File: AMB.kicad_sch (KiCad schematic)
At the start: 14 parts, among them U11 EPC2152, U12 EPC2152

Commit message: updated layouts, added motor
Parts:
- renumbered C95 to C119, C96 to C120, C97 to C121, C98 to C122, C99 to C123, C100 to C124, C101 to C125, C102 to C126, R71 to R127, R72 to R128, R73 to R129, R74 to R130, U12 to U10, U11 to U9

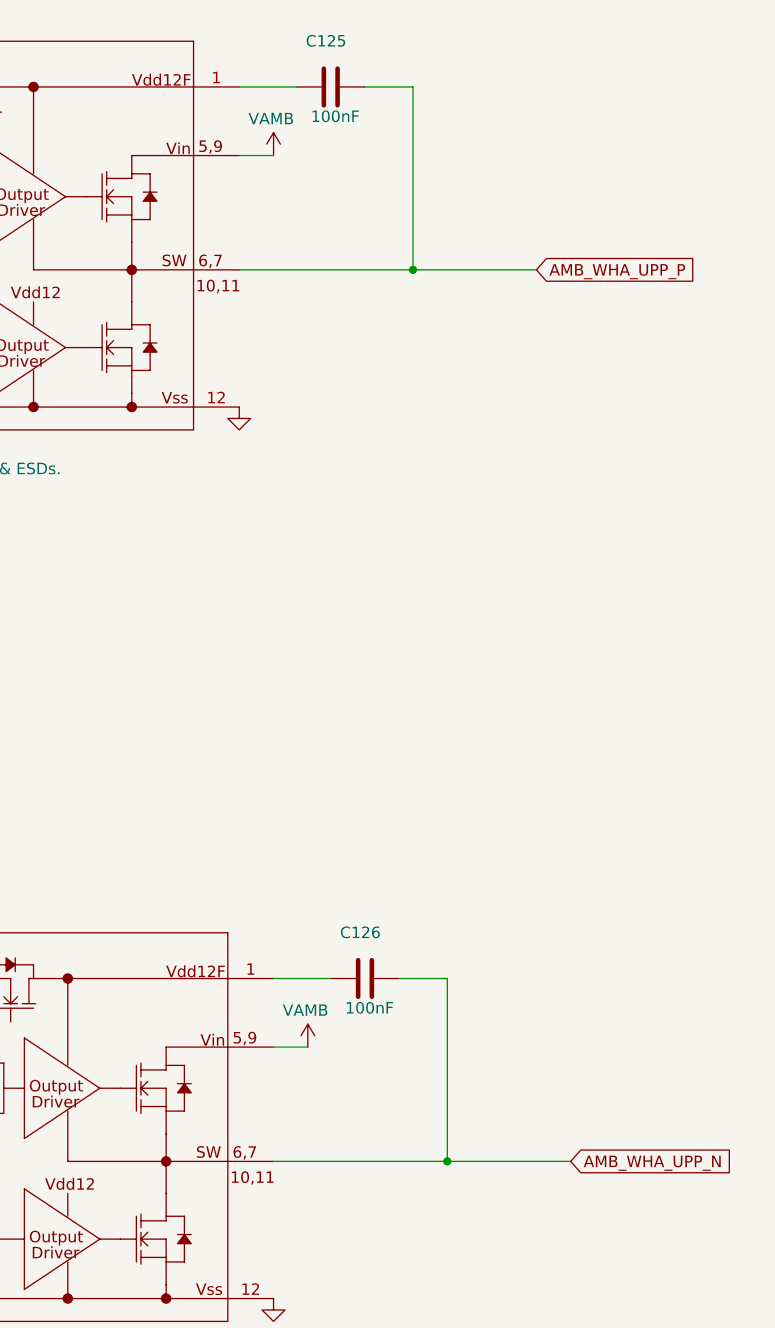
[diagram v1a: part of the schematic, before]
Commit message: Changes to layout pins
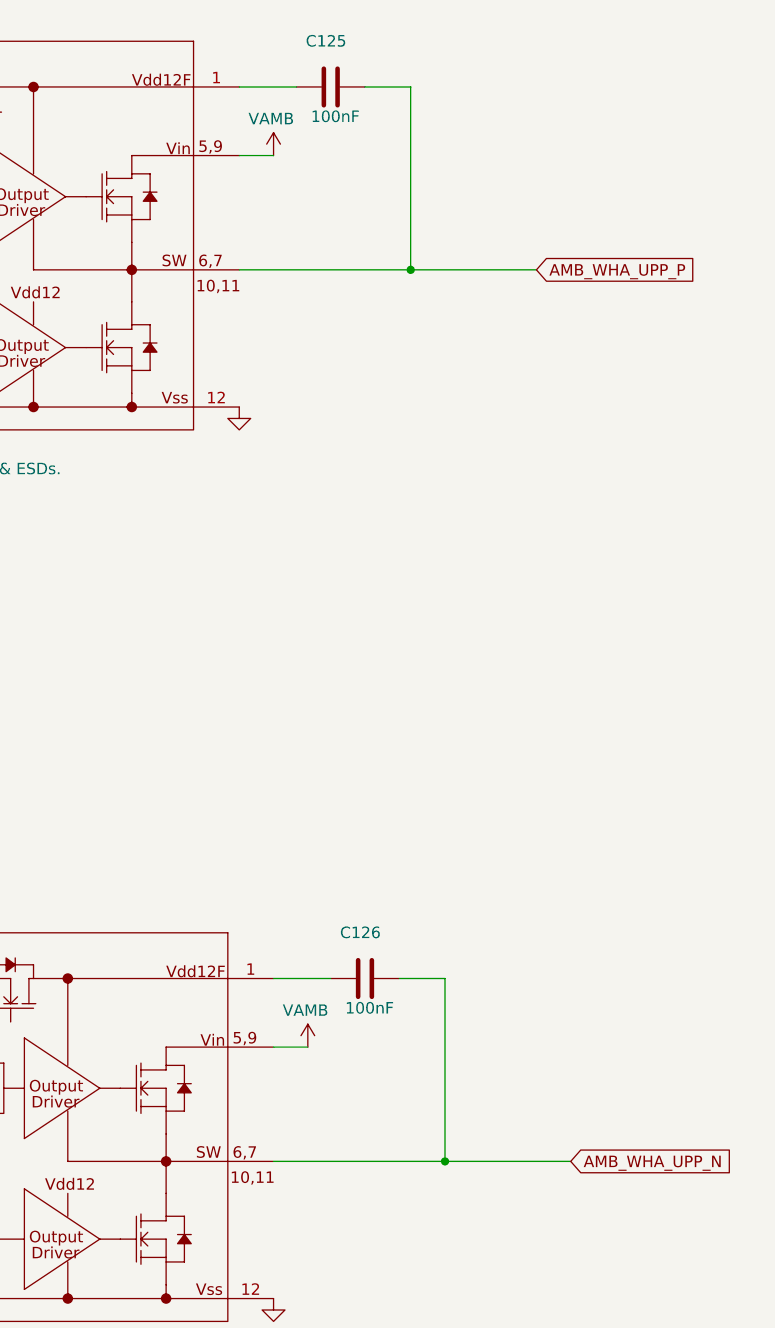
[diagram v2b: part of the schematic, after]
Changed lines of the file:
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@@
 	)
 	(junction
-		(at 184.404 154.94)
+		(at 184.15 154.94)
 		(diameter 0)
 		(color 0 0 0 0)
 	)
 	(junction
-		(at 180.594 55.88)
+		(at 180.34 55.88)
 		(diameter 0)
 		(color 0 0 0 0)
@@
 	(wire
 		(pts
-			(xy 184.404 154.94) (xy 198.12 154.94)
+			(xy 184.15 154.94) (xy 198.12 154.94)
 		)
 		(stroke
@@
 	(wire
 		(pts
-			(xy 161.29 55.88) (xy 180.594 55.88)
+			(xy 161.29 55.88) (xy 180.34 55.88)
 		)
 		(stroke
@@
 	(wire
 		(pts
-			(xy 180.594 55.88) (xy 194.31 55.88)
+			(xy 180.34 55.88) (xy 194.31 55.88)
 		)
 		(stroke
@@
 	(wire
 		(pts
-			(xy 184.404 134.62) (xy 184.404 154.94)
+			(xy 184.15 134.62) (xy 184.15 154.94)
 		)
 		(stroke
@@
 	(wire
 		(pts
-			(xy 180.594 35.56) (xy 180.594 55.88)
+			(xy 180.34 35.56) (xy 180.34 55.88)
 		)
 		(stroke
@@
 	(wire
 		(pts
-			(xy 179.07 134.62) (xy 184.404 134.62)
+			(xy 179.07 134.62) (xy 184.15 134.62)
 		)
 		(stroke
@@
 	(wire
 		(pts
-			(xy 165.1 154.94) (xy 184.404 154.94)
+			(xy 165.1 154.94) (xy 184.15 154.94)
 		)
 		(stroke
@@
 	(wire
 		(pts
-			(xy 175.26 35.56) (xy 180.594 35.56)
+			(xy 175.26 35.56) (xy 180.34 35.56)
 		)
 		(stroke
@@
 	)
 	(symbol
-		(lib_id "CIAA_ACC:GND")
+		(lib_id "power:GND")
 		(at 161.29 71.12 0)
 		(unit 1)
@@
 		(property "Footprint" ""
 			(at 161.29 71.12 0)
+			(hide yes)
 			(show_name no)
 			(do_not_autoplace no)
@@
 		(property "Datasheet" ""
 			(at 161.29 71.12 0)
+			(hide yes)
 			(show_name no)
 			(do_not_autoplace no)
@@
 			)
 		)
-		(property "Description" ""
+		(property "Description" "Power symbol creates a global label with name \"GND\" , ground"
 			(at 161.29 71.12 0)
+			(hide yes)
 			(show_name no)
 			(do_not_autoplace no)
@@
 	)
 	(symbol
-		(lib_id "CIAA_ACC:GND")
+		(lib_id "power:GND")
 		(at 72.39 54.61 0)
 		(unit 1)
@@
 		(property "Footprint" ""
 			(at 72.39 54.61 0)
+			(hide yes)
 			(show_name no)
 			(do_not_autoplace no)
@@
 		(property "Datasheet" ""
 			(at 72.39 54.61 0)
+			(hide yes)
 			(show_name no)
 			(do_not_autoplace no)
@@
 			)
 		)
-		(property "Description" ""
+		(property "Description" "Power symbol creates a global label with name \"GND\" , ground"
 			(at 72.39 54.61 0)
+			(hide yes)
 			(show_name no)
 			(do_not_autoplace no)
@@
 	)
 	(symbol
-		(lib_id "CIAA_ACC:GND")
+		(lib_id "power:GND")
 		(at 95.25 44.45 0)
 		(unit 1)
@@
 		(property "Footprint" ""
 			(at 95.25 44.45 0)
+			(hide yes)
 			(show_name no)
 			(do_not_autoplace no)
@@
 		(property "Datasheet" ""
 			(at 95.25 44.45 0)
+			(hide yes)
 			(show_name no)
 			(do_not_autoplace no)
@@
 			)
 		)
-		(property "Description" ""
+		(property "Description" "Power symbol creates a global label with name \"GND\" , ground"
 			(at 95.25 44.45 0)
+			(hide yes)
 			(show_name no)
 			(do_not_autoplace no)
@@
 	)
 	(symbol
-		(lib_id "CIAA_ACC:GND")
+		(lib_id "power:GND")
 		(at 100.33 71.12 0)
 		(unit 1)
@@
 		(property "Footprint" ""
 			(at 100.33 71.12 0)
+			(hide yes)
 			(show_name no)
 			(do_not_autoplace no)
@@
 		(property "Datasheet" ""
 			(at 100.33 71.12 0)
+			(hide yes)
 			(show_name no)
 			(do_not_autoplace no)
@@
 			)
 		)
-		(property "Description" ""
+		(property "Description" "Power symbol creates a global label with name \"GND\" , ground"
 			(at 100.33 71.12 0)
+			(hide yes)
 			(show_name no)
 			(do_not_autoplace no)
@@
 	)
 	(symbol
-		(lib_id "CIAA_ACC:GND")
+		(lib_id "power:GND")
 		(at 165.1 170.18 0)
 		(unit 1)
@@
 		(property "Footprint" ""
 			(at 165.1 170.18 0)
+			(hide yes)
 			(show_name no)
 			(do_not_autoplace no)
@@
 		(property "Datasheet" ""
 			(at 165.1 170.18 0)
+			(hide yes)
 			(show_name no)
 			(do_not_autoplace no)
@@
 			)
 		)
-		(property "Description" ""
+		(property "Description" "Power symbol creates a global label with name \"GND\" , ground"
 			(at 165.1 170.18 0)
+			(hide yes)
 			(show_name no)
 			(do_not_autoplace no)
@@
 	)
 	(symbol
-		(lib_id "CIAA_ACC:GND")
+		(lib_id "power:GND")
 		(at 43.18 102.87 0)
 		(unit 1)
@@
 		(property "Footprint" ""
 			(at 43.18 102.87 0)
+			(hide yes)
 			(show_name no)
 			(do_not_autoplace no)
@@
 		(property "Datasheet" ""
 			(at 43.18 102.87 0)
+			(hide yes)
 			(show_name no)
 			(do_not_autoplace no)
@@
 			)
 		)
-		(property "Description" ""
+		(property "Description" "Power symbol creates a global label with name \"GND\" , ground"
 			(at 43.18 102.87 0)
+			(hide yes)
 			(show_name no)
 			(do_not_autoplace no)
@@
 	)
 	(symbol
-		(lib_id "CIAA_ACC:GND")
+		(lib_id "power:GND")
 		(at 76.2 153.67 0)
 		(unit 1)
@@
 		(property "Footprint" ""
 			(at 76.2 153.67 0)
+			(hide yes)
 			(show_name no)
 			(do_not_autoplace no)
@@
 		(property "Datasheet" ""
 			(at 76.2 153.67 0)
+			(hide yes)
 			(show_name no)
 			(do_not_autoplace no)
@@
 			)
 		)
-		(property "Description" ""
+		(property "Description" "Power symbol creates a global label with name \"GND\" , ground"
 			(at 76.2 153.67 0)
+			(hide yes)
 			(show_name no)
 			(do_not_autoplace no)
@@
 	)
 	(symbol
-		(lib_id "CIAA_ACC:GND")
+		(lib_id "power:GND")
 		(at 68.58 69.85 0)
 		(unit 1)
@@
 		(property "Footprint" ""
 			(at 68.58 69.85 0)
+			(hide yes)
 			(show_name no)
 			(do_not_autoplace no)
@@
 		(property "Datasheet" ""
 			(at 68.58 69.85 0)
+			(hide yes)
 			(show_name no)
 			(do_not_autoplace no)
@@
 			)
 		)
-		(property "Description" ""
+		(property "Description" "Power symbol creates a global label with name \"GND\" , ground"
 			(at 68.58 69.85 0)
+			(hide yes)
 			(show_name no)
 			(do_not_autoplace no)
@@
 	)
 	(symbol
-		(lib_id "CIAA_ACC:GND")
+		(lib_id "power:GND")
 		(at 104.14 170.18 0)
 		(unit 1)
@@
 		(property "Footprint" ""
 			(at 104.14 170.18 0)
+			(hide yes)
 			(show_name no)
 			(do_not_autoplace no)
@@
 		(property "Datasheet" ""
 			(at 104.14 170.18 0)
+			(hide yes)
 			(show_name no)
 			(do_not_autoplace no)
@@
 			)
 		)
-		(property "Description" ""
+		(property "Description" "Power symbol creates a global label with name \"GND\" , ground"
 			(at 104.14 170.18 0)
+			(hide yes)
 			(show_name no)
 			(do_not_autoplace no)
@@
 	)
 	(symbol
-		(lib_id "CIAA_ACC:GND")
+		(lib_id "power:GND")
 		(at 99.06 143.51 0)
 		(unit 1)
@@
 		(property "Footprint" ""
 			(at 99.06 143.51 0)
+			(hide yes)
 			(show_name no)
 			(do_not_autoplace no)
@@
 		(property "Datasheet" ""
 			(at 99.06 143.51 0)
+			(hide yes)
 			(show_name no)
 			(do_not_autoplace no)
@@
 			)
 		)
-		(property "Description" ""
+		(property "Description" "Power symbol creates a global label with name \"GND\" , ground"
 			(at 99.06 143.51 0)
+			(hide yes)
 			(show_name no)
 			(do_not_autoplace no)
@@
 	)
 	(symbol
-		(lib_id "CIAA_ACC:GND")
+		(lib_id "power:GND")
 		(at 72.39 168.91 0)
 		(unit 1)
@@
 		(property "Footprint" ""
 			(at 72.39 168.91 0)
+			(hide yes)
 			(show_name no)
 			(do_not_autoplace no)
@@
 		(property "Datasheet" ""
 			(at 72.39 168.91 0)
+			(hide yes)
 			(show_name no)
 			(do_not_autoplace no)
@@
 			)
 		)
-		(property "Description" ""
+		(property "Description" "Power symbol creates a global label with name \"GND\" , ground"
 			(at 72.39 168.91 0)
+			(hide yes)
 			(show_name no)
 			(do_not_autoplace no)
